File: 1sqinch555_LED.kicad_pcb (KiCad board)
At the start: 2 copper layers, 24.7 x 24 mm, 15 parts, among them J11 Conn_01x01, J25 Conn_01x01, J30 Conn_01x01, J31 Conn_01x01, J7 Conn_01x01, J9 Conn_01x01

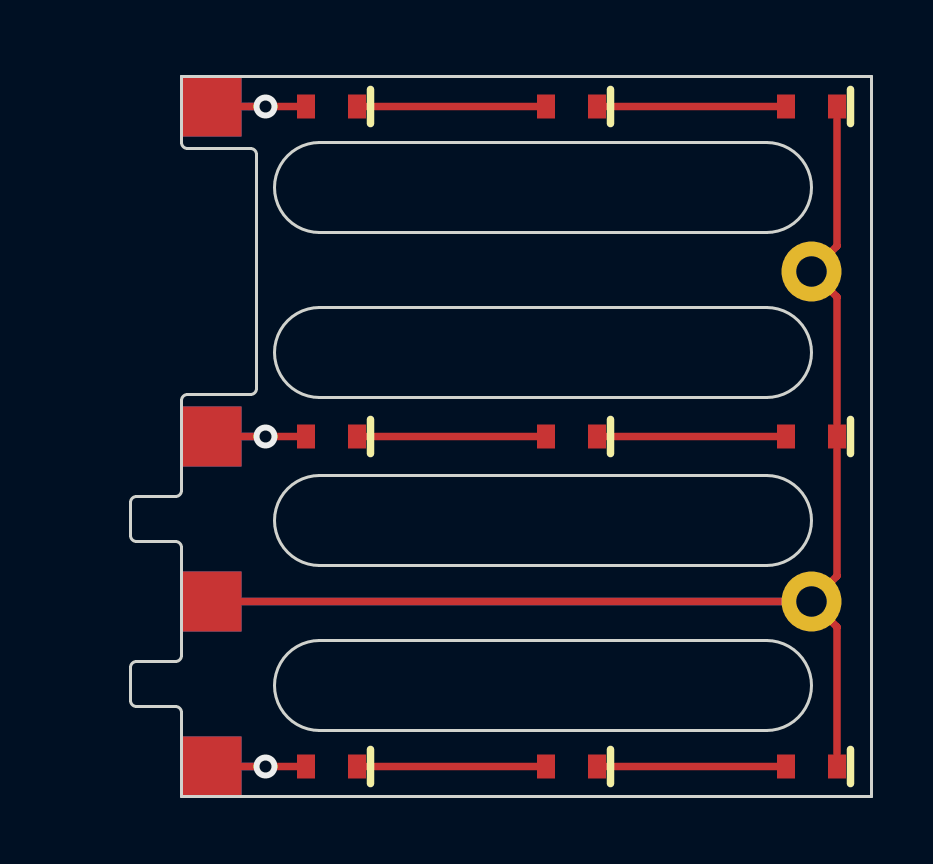
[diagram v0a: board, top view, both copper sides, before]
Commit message: changed 0603 to 0805
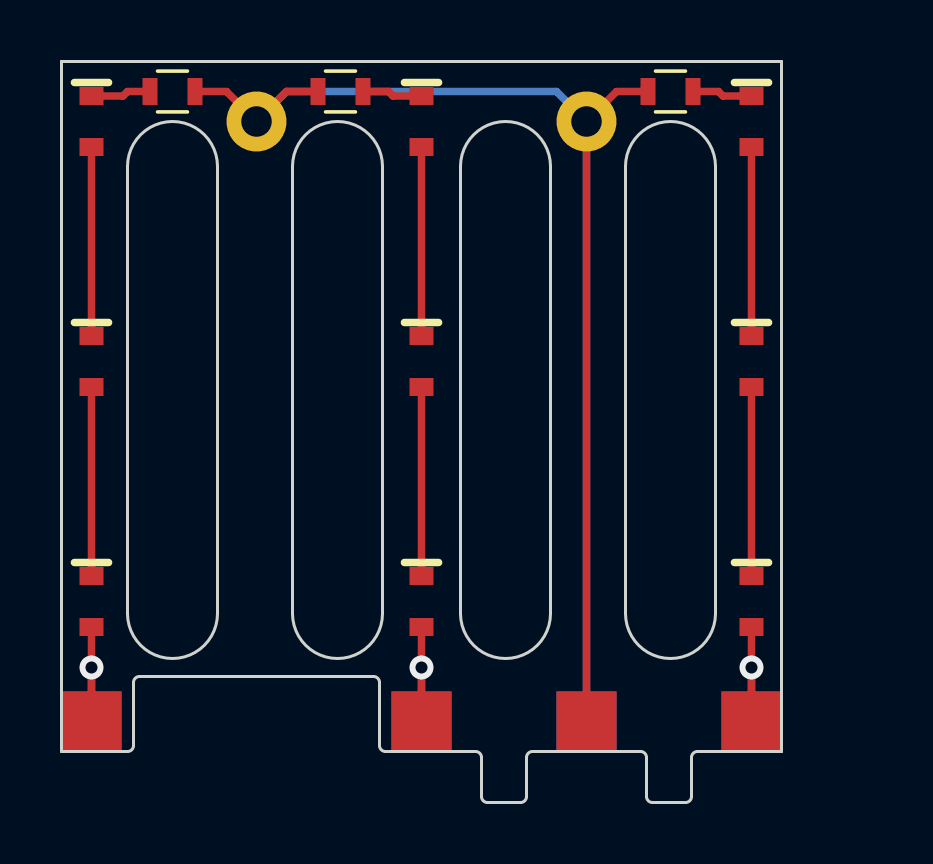
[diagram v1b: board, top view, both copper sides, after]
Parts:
- added R2: 300, 1sqinch555_fp:R_0603, F.Cu at (68.7, 38.5)
- added R3: 300, 1sqinch555_fp:R_0603, F.Cu at (74.3, 38.5)
- added R4: 300, 1sqinch555_fp:R_0603, F.Cu at (85.3, 38.5)
- moved D3 24.0 mm to (66.0, 39.5), turned to 270 degrees
- moved D9 21.6 mm to (88.0, 39.5), turned to 270 degrees
- moved J7 20.9 mm to (66.0, 59.5), turned to 90 degrees
- moved J30 19.2 mm to (71.5, 39.5), turned to 90 degrees
- moved D1 18.3 mm to (66.0, 55.5), turned to 270 degrees
- moved D2 18.1 mm to (66.0, 47.5), turned to 270 degrees
- moved J11 18.1 mm to (88.0, 59.5), turned to 90 degrees
- moved J31 17.7 mm to (82.5, 39.5), turned to 90 degrees
- moved D6 16.7 mm to (77.0, 39.5), turned to 270 degrees
- moved D7 15.0 mm to (88.0, 55.5), turned to 270 degrees
- moved D8 14.8 mm to (88.0, 47.5), turned to 270 degrees
- moved J25 13.1 mm to (82.5, 59.5), turned to 90 degrees
- moved J9 11.8 mm to (77.0, 59.5), turned to 90 degrees
- moved D4 6.26 mm to (77.0, 55.5), turned to 270 degrees
- moved D5 5.59 mm to (77.0, 47.5), turned to 270 degrees
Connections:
- D3 pad 1: /GND1 -> Net-(D3-Pad1)
- D6 pad 1: /GND1 -> Net-(D6-Pad1)
- D9 pad 1: /GND1 -> Net-(D9-Pad1)
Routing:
- net /GND1: track 63.4 -> 59.2 mm
- net Net-(D9-Pad1): track 0.00 -> 2.01 mm
- net Net-(D6-Pad1): track 0.00 -> 2.01 mm
- net Net-(D3-Pad1): track 0.00 -> 2.01 mm
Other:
- board size 24.7 x 24 mm -> 24 x 24.7 mm

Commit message: layout changes
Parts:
- D1, D2, D3, D4, D5, D6, D7, D8, D9: footprint 1sqinch555_fp:D_0603 -> 1sqinch555_fp:LED-0805
- R2, R3, R4: footprint 1sqinch555_fp:R_0603 -> 1sqinch555_fp:R_0805
- moved J30 1.50 mm to (71.5, 41.0)
- moved J31 1.50 mm to (82.5, 41.0)
- moved R2 0.70 mm to (69.4, 38.5)
- moved R4 0.70 mm to (84.6, 38.5)
- moved R3 0.50 mm to (73.8, 38.5)
- moved D2 0.20 mm to (66.2, 47.5)
- moved D8 0.20 mm to (87.8, 47.5)
- moved D1 0.20 mm to (66.2, 55.5)
- moved D3 0.20 mm to (66.2, 39.5)
- moved D7 0.20 mm to (87.8, 55.5)
- moved D9 0.20 mm to (87.8, 39.5)
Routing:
- net /GND1: track 59.2 -> 41.3 mm, vias 0 -> 1
- net /7: track 4.95 -> 2.95 mm
- net /10: track 4.95 -> 3.03 mm
- net /11: track 4.95 -> 3.03 mm
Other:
- outline, holes or cut-outs redrawn
